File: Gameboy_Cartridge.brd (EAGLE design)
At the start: 51 x 48 mm, 4 parts, among them IC1 AT49F040J

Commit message: Files sent to manufacture
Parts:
- added C1: 20nF, resistor:C0805
- R1: value 47000 -> 47K
- moved R1 45.3 mm to (40.0, 41.6), turned to 180 degrees
- moved IC1 5.52 mm to (38.1, 30.3)
- moved U$2 2.20 mm to (18.9, 23.4)
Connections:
- new net 31: IC1.31, R1.1, U$1.31
- net A: now also IC1.1, U$2.14; no longer IC1.2, U$2.16
- net B: now also IC1.30, U$2.15; no longer IC1.3, U$2.17
- net C: now also IC1.2, U$2.16; no longer IC1.31, R1.1, U$1.31, U$2.14
- net D: now also IC1.3, U$2.17; no longer IC1.30, U$2.15
- net GND: now also C1.2; no longer IC1.1
- net VDD: now also C1.1
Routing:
- net 19: track 0.00 -> 84.5 mm, vias 0 -> 3
- net VDD: track 0.00 -> 81.2 mm
- net 21: track 0.00 -> 78.7 mm
- net 14: track 0.00 -> 68.9 mm, vias 0 -> 2
- net 4: track 0.00 -> 66.5 mm, vias 0 -> 3
- net 30: track 0.00 -> 61.7 mm, vias 0 -> 2
- net GND: track 0.00 -> 59.0 mm, vias 0 -> 4
- net 8: track 0.00 -> 58.2 mm
- net 20: track 0.00 -> 49.4 mm, vias 0 -> 2
- net 26: track 0.00 -> 44.0 mm
- net 18: track 0.00 -> 43.1 mm, vias 0 -> 2
- net 31: track 0.00 -> 42.7 mm
- net 25: track 0.00 -> 42.3 mm
- net E: track 0.00 -> 40.6 mm, vias 0 -> 2
- net 24: track 0.00 -> 40.3 mm
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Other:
- board size 51 x 48 mm -> 49.3 x 48 mm
- board text added: "47417"
- board text added: "Cartridge"
- board text added: "Gameboy"
- board text added: "Homebrew"
- board text added: "goo.gl/Hq5Kc"

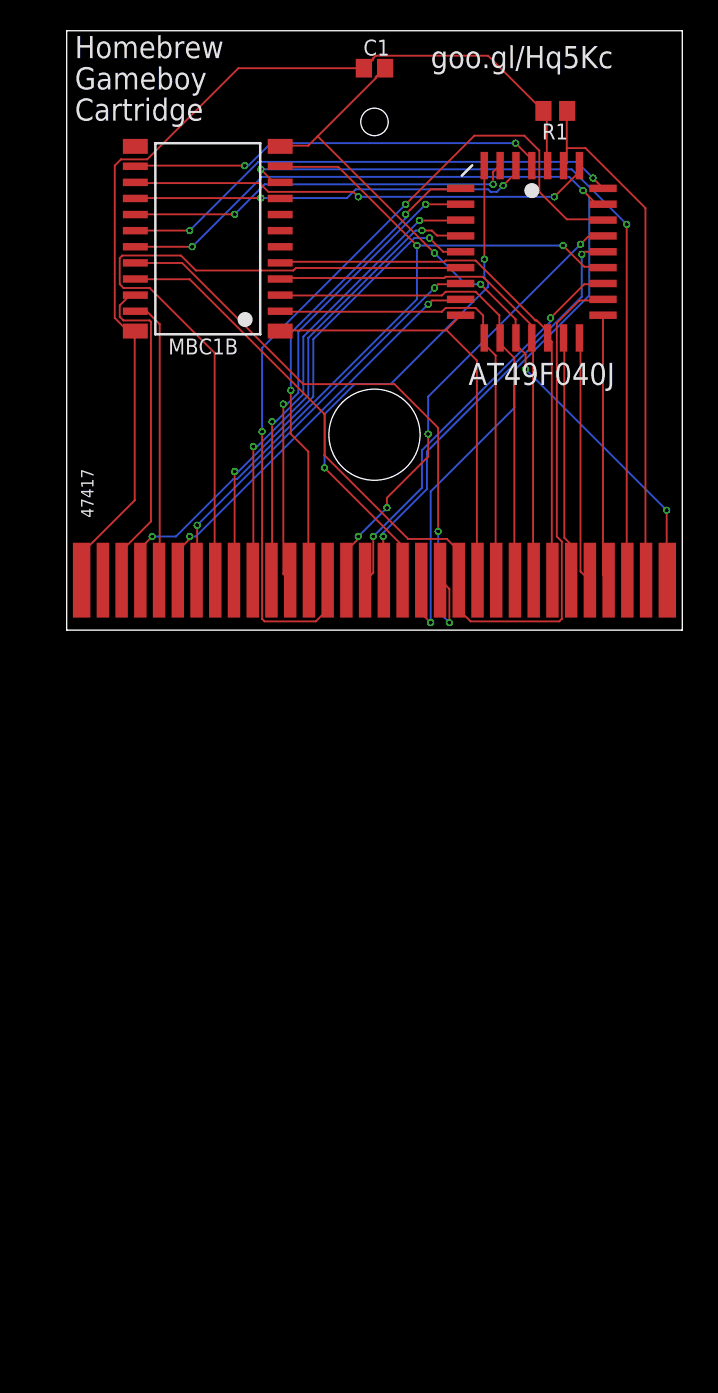
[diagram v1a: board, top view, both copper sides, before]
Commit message: add solder jumpers where traces should be shorted for ROM only operation
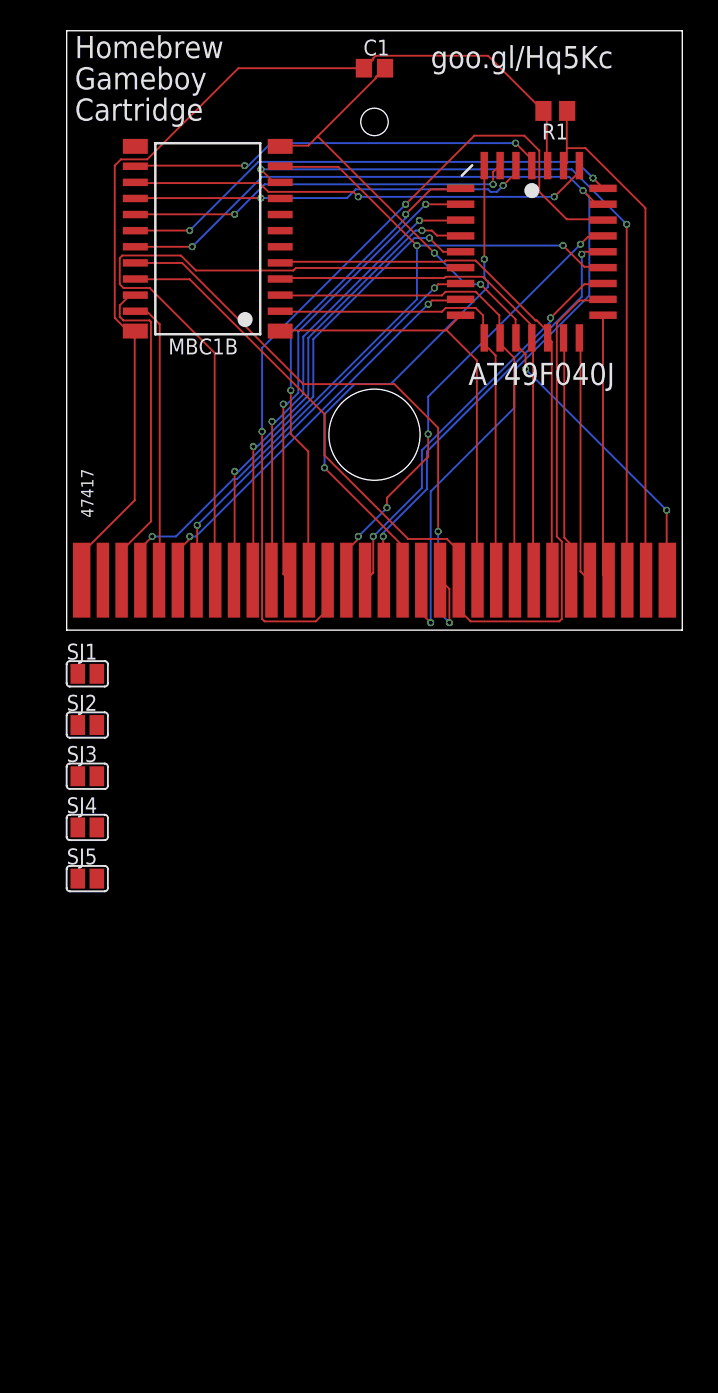
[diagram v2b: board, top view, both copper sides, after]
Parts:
- added SJ1, SJ2, SJ3, SJ4, SJ5: (no value), jumper:SJ
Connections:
- net A: now also SJ1.1
- net B: now also SJ2.1, SJ3.1, SJ4.1
- net GND: now also SJ1.2, SJ2.2, SJ3.2, SJ4.2
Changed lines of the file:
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@@
 <?xml version="1.0" encoding="utf-8"?>
 <!DOCTYPE eagle SYSTEM "eagle.dtd">
-<eagle version="6.1">
+<eagle version="9.3.2">
 <drawing>
 <settings>
 <setting alwaysvectorfont="no"/>
+<setting keepoldvectorfont="yes"/>
 <setting verticaltext="up"/>
 </settings>
@@
 </class>
 </classes>
-<designrules>
+<designrules name="default">
 <description language="de">&lt;b&gt;EAGLE Design Rules&lt;/b&gt;
 &lt;p&gt;
@@
 <param name="dpMaxLengthDifference" value="10mm"/>
 <param name="dpGapFactor" value="2.5"/>
-<param name="checkGrid" value="0"/>
 <param name="checkAngle" value="0"/>
 <param name="checkFont" value="1"/>
 <param name="checkRestrict" value="0"/>
+<param name="checkStop" value="0"/>
+<param name="checkValues" value="0"/>
+<param name="checkNames" value="1"/>
+<param name="checkWireStubs" value="1"/>
+<param name="checkPolygonWidth" value="0"/>
 <param name="useDiameter" value="13"/>
 <param name="maxErrors" value="50"/>
@@
 <pass name="Default">
 <param name="RoutingGrid" value="0.1mm"/>
+<param name="AutoGrid" value="1"/>
+<param name="Efforts" value="0"/>
+<param name="TopRouterVariant" value="1"/>
 <param name="tpViaShape" value="round"/>
 <param name="PrefDir.1" value="*"/>
@@
 </autorouter>
 <elements>
-<element name="U$2" library="gameboy" package="MBC1B" value="MBC1B" x="18.95" y="23.35" rot="R180"/>
-<element name="U$1" library="gameboy" package="CONNECTOR" value="CONNECTOR" x="1.35" y="7"/>
-<element name="R1" library="resistor" package="M0805" value="47K" x="39.98" y="41.58" rot="R180"/>
-<element name="IC1" library="gameboy" package="PLCC32R" value="AT49F040J" x="38.1" y="30.3"/>
-<element name="C1" library="resistor" package="C0805" value="20nF" x="25.5" y="45"/>
+<element name="U$2" library="gameboy" package="MBC1B" value="MBC1B" x="18.95" y="23.35" smashed="yes" rot="R180">
+<attribute name="VALUE" x="14.579996875" y="23.35" size="1.27" layer="21" rot="R180"/>
+</element>
+<element name="U$1" library="gameboy" package="CONNECTOR" value="CONNECTOR" x="1.35" y="7" smashed="yes"/>
+<element name="R1" library="resistor" package="M0805" value="47K" x="39.98" y="41.58" smashed="yes" rot="R180">
+<attribute name="NAME" x="40.996" y="40.564" size="1.27" layer="25" rot="R180"/>
+<attribute name="VALUE" x="40.996" y="43.866" size="1.27" layer="27" rot="R180"/>
+</element>
+<element name="IC1" library="gameboy" package="PLCC32R" value="AT49F040J" x="38.1" y="30.3" smashed="yes">
+<attribute name="VALUE" x="33.02" y="19.632" size="1.778" layer="21"/>
+</element>
+<element name="C1" library="resistor" package="C0805" value="20nF" x="25.5" y="45" smashed="yes">
+<attribute name="NAME" x="24.611" y="46.016" size="1.27" layer="25"/>
+<attribute name="VALUE" x="24.611" y="42.714" size="1.27" layer="27"/>
+</element>
+<element name="SJ1" library="jumper" library_urn="urn:adsk.eagle:library:252" package="SJ" package3d_urn="urn:adsk.eagle:package:15471/1" value="" x="2.5" y="-3.5" smashed="yes">
+<attribute name="NAME" x="0.849" y="-2.357" size="1.27" layer="25" ratio="10"/>
+<attribute name="VALUE" x="2.9001" y="-3.5" size="0.02" layer="27"/>
+</element>
+<element name="SJ2" library="jumper" library_urn="urn:adsk.eagle:library:252" package="SJ" package3d_urn="urn:adsk.eagle:package:15471/1" value="" x="2.5" y="-7.6" smashed="yes">
+<attribute name="NAME" x="0.849" y="-6.457" size="1.27" layer="25" ratio="10"/>
+<attribute name="VALUE" x="2.9001" y="-7.6" size="0.02" layer="27"/>
+</element>
+<element name="SJ3" library="jumper" library_urn="urn:adsk.eagle:library:252" package="SJ" package3d_urn="urn:adsk.eagle:package:15471/1" value="" x="2.5" y="-11.7" smashed="yes">
+<attribute name="NAME" x="0.849" y="-10.557" size="1.27" layer="25" ratio="10"/>
+<attribute name="VALUE" x="2.9001" y="-11.7" size="0.02" layer="27"/>
+</element>
+<element name="SJ4" library="jumper" library_urn="urn:adsk.eagle:library:252" package="SJ" package3d_urn="urn:adsk.eagle:package:15471/1" value="" x="2.5" y="-15.8" smashed="yes">
+<attribute name="NAME" x="0.849" y="-14.657" size="1.27" layer="25" ratio="10"/>
+<attribute name="VALUE" x="2.9001" y="-15.8" size="0.02" layer="27"/>
+</element>
+<element name="SJ5" library="jumper" library_urn="urn:adsk.eagle:library:252" package="SJ" package3d_urn="urn:adsk.eagle:package:15471/1" value="" x="2.5" y="-19.9" smashed="yes">
+<attribute name="NAME" x="0.849" y="-18.757" size="1.27" layer="25" ratio="10"/>
+<attribute name="VALUE" x="2.9001" y="-19.9" size="0.02" layer="27"/>
+</element>
 </elements>
 <signals>
@@
 <via x="48.9" y="9.6" extent="1-16" drill="0.3048"/>
 <via x="37.6" y="20.9" extent="1-16" drill="0.3048"/>
+<contactref element="SJ1" pad="2"/>
+<contactref element="SJ3" pad="2"/>
+<contactref element="SJ4" pad="2"/>
+<contactref element="SJ2" pad="2"/>
+<wire x1="3.262" y1="-3.5" x2="37.6" y2="20.9" width="0" layer="19" extent="1-1"/>
+<wire x1="3.262" y1="-7.6" x2="3.262" y2="-3.5" width="0" layer="19" extent="1-1"/>
+<wire x1="3.262" y1="-11.7" x2="3.262" y2="-7.6" width="0" layer="19" extent="1-1"/>
+<wire x1="3.262" y1="-15.8" x2="3.262" y2="-11.7" width="0" layer="19" extent="1-1"/>
 </signal>
 <signal name="VDD">
@@
 <via x="24.2" y="34.7" extent="1-16" drill="0.3048"/>
 <via x="39.9" y="34.7" extent="1-16" drill="0.3048"/>
+<contactref element="SJ2" pad="1"/>
+<contactref element="SJ3" pad="1"/>
+<contactref element="SJ4" pad="1"/>
+<wire x1="1.738" y1="-7.6" x2="6.4" y2="35.8" width="0" layer="19" extent="1-1"/>
+<wire x1="1.738" y1="-11.7" x2="1.738" y2="-7.6" width="0" layer="19" extent="1-1"/>
+<wire x1="1.738" y1="-15.8" x2="1.738" y2="-11.7" width="0" layer="19" extent="1-1"/>
 </signal>
 <signal name="A">
@@
 <via x="15.1" y="37.2" extent="1-16" drill="0.3048"/>
 <via x="36.8" y="39" extent="1-16" drill="0.3048"/>
+<contactref element="SJ1" pad="1"/>
+<wire x1="1.738" y1="-3.5" x2="6.35" y2="37.15" width="0" layer="19" extent="1-1"/>
 </signal>
 </signals>
+<mfgpreviewcolors>
+<mfgpreviewcolor name="soldermaskcolor" color="0xC8008000"/>
+<mfgpreviewcolor name="silkscreencolor" color="0xFFFEFEFE"/>
+<mfgpreviewcolor name="backgroundcolor" color="0xFF282828"/>
+<mfgpreviewcolor name="coppercolor" color="0xFFFFBF00"/>
+<mfgpreviewcolor name="substratecolor" color="0xFF786E46"/>
+</mfgpreviewcolors>
 </board>
 </drawing>
+<compatibility>
+<note version="8.2" severity="warning">
+Since Version 8.2, EAGLE supports online libraries. The ids
+of those online libraries will not be understood (or retained)
+with this version.
+</note>
+<note version="8.3" severity="warning">
+Since Version 8.3, EAGLE supports URNs for individual library
+assets (packages, symbols, and devices). The URNs of those assets
+will not be understood (or retained) with this version.
+</note>
+<note version="8.3" severity="warning">
+Since Version 8.3, EAGLE supports the association of 3D packages
+with devices in libraries, schematics, and board files. Those 3D
+packages will not be understood (or retained) with this version.
+</note>
+</compatibility>
 </eagle>

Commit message: replace the solder jumper with my new part
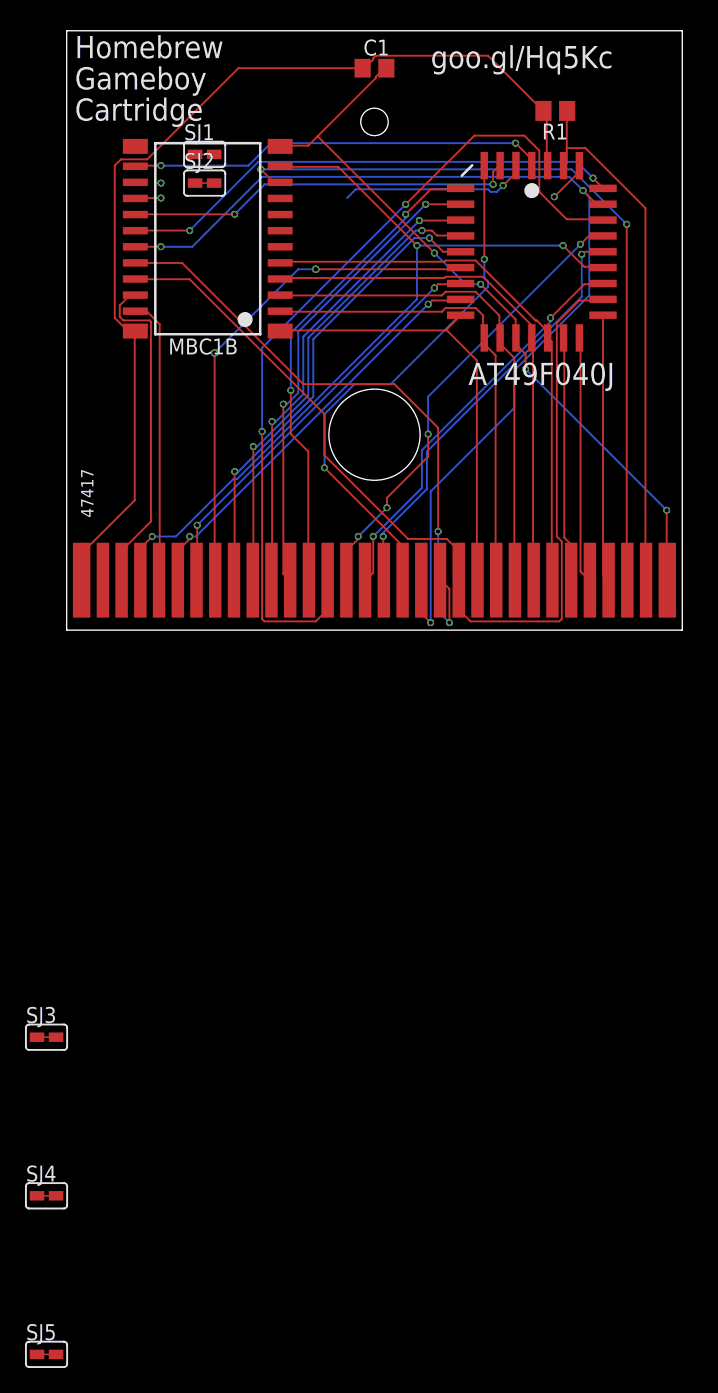
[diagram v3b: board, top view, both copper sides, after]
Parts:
- SJ1, SJ2, SJ3, SJ4, SJ5: value (none) -> SOLDER-JUMPER; device jumper:SJ -> gameboy:SJ
- moved SJ2 44.4 mm to (11.9, 35.8)
- moved SJ1 42.6 mm to (11.9, 38.1)
- moved SJ5 38.2 mm to (-0.76, -58.0)
- moved SJ4 29.7 mm to (-0.76, -45.3)
- moved SJ3 21.2 mm to (-0.76, -32.6)
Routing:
- net B: track 37.4 -> 3.42 mm
- net 8: track 58.2 -> 40.8 mm, vias 0 -> 2
- net C: track 32.1 -> 17.2 mm

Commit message: Fix the connections on the solder jumper
No ERC errors
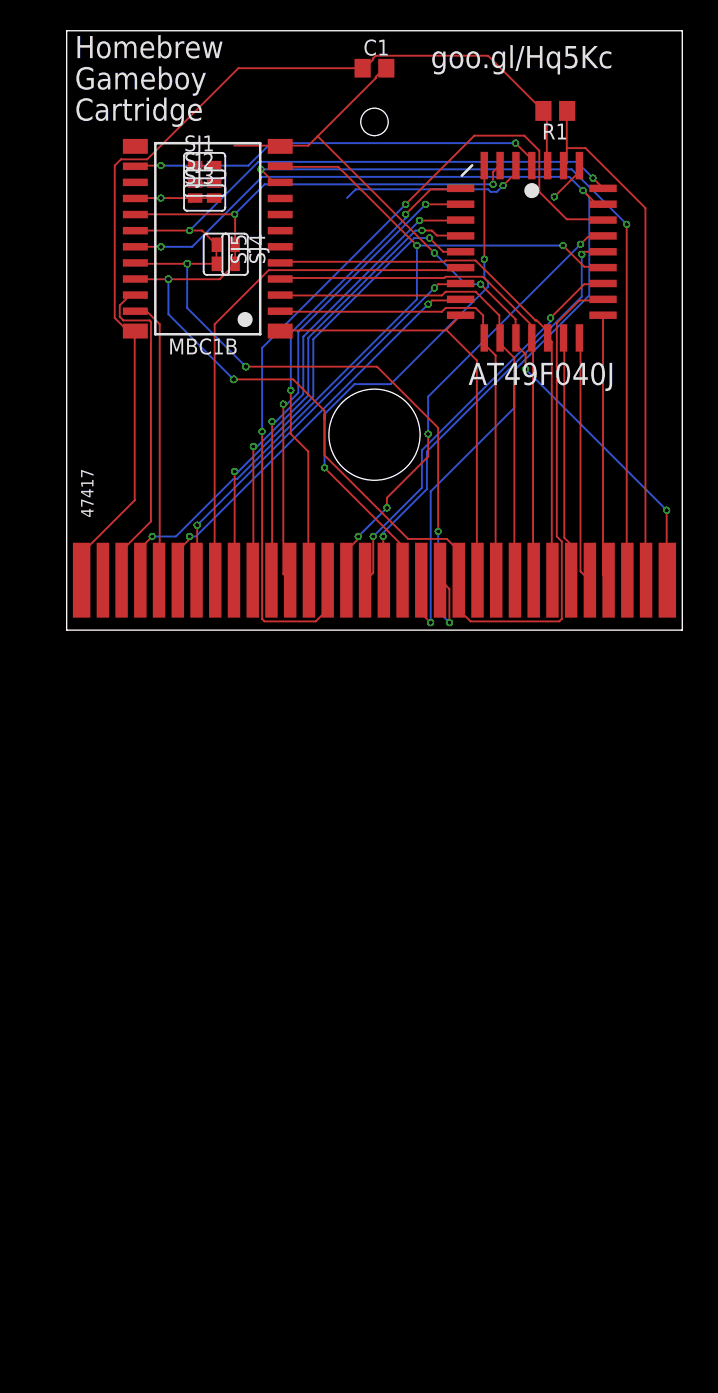
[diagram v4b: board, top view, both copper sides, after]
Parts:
- moved SJ5 89.1 mm to (12.8, 30.1), turned to 270 degrees
- moved SJ4 76.9 mm to (14.3, 30.1), turned to 270 degrees
- moved SJ3 68.4 mm to (11.9, 34.6)
- moved SJ1 0.90 mm to (11.9, 37.2)
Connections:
- net 20: now also SJ5.2
- net 21: now also SJ4.2
- net B: no longer SJ3.1, SJ4.1
- net C: now also SJ3.1
- net D: now also SJ4.1
- net E: now also SJ5.1
- net GND: no longer SJ4.2
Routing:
- net 21: track 78.7 -> 86.8 mm, vias 0 -> 2
- net 20: track 49.4 -> 53.9 mm, vias 2 -> 4
- net GND: track 59.1 -> 62.8 mm
- net C: track 17.2 -> 19.9 mm
- net E: track 40.6 -> 43.2 mm
- net D: track 31.4 -> 33.9 mm
- net 8: track 40.8 -> 42.4 mm, vias 2 -> 0
- net B: vias 2 -> 1

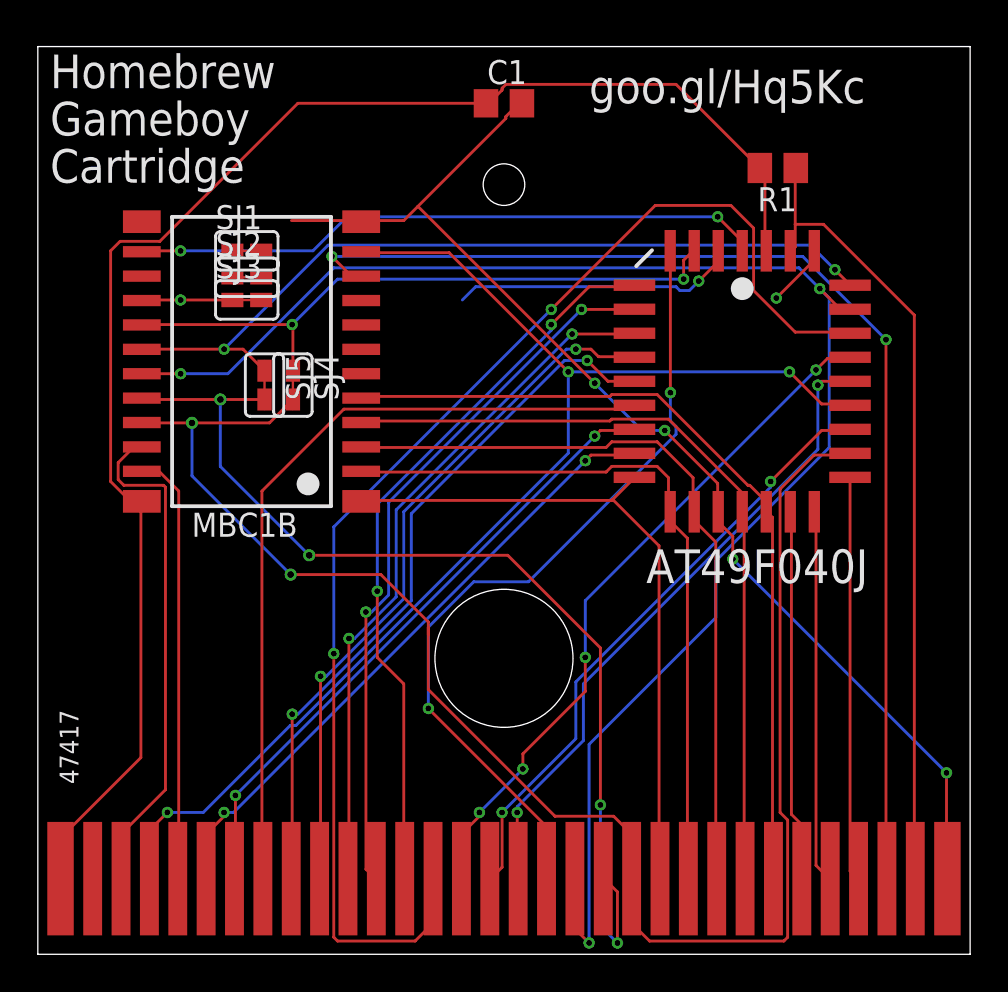
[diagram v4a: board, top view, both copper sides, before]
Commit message: Ripup all traces. Route most of it
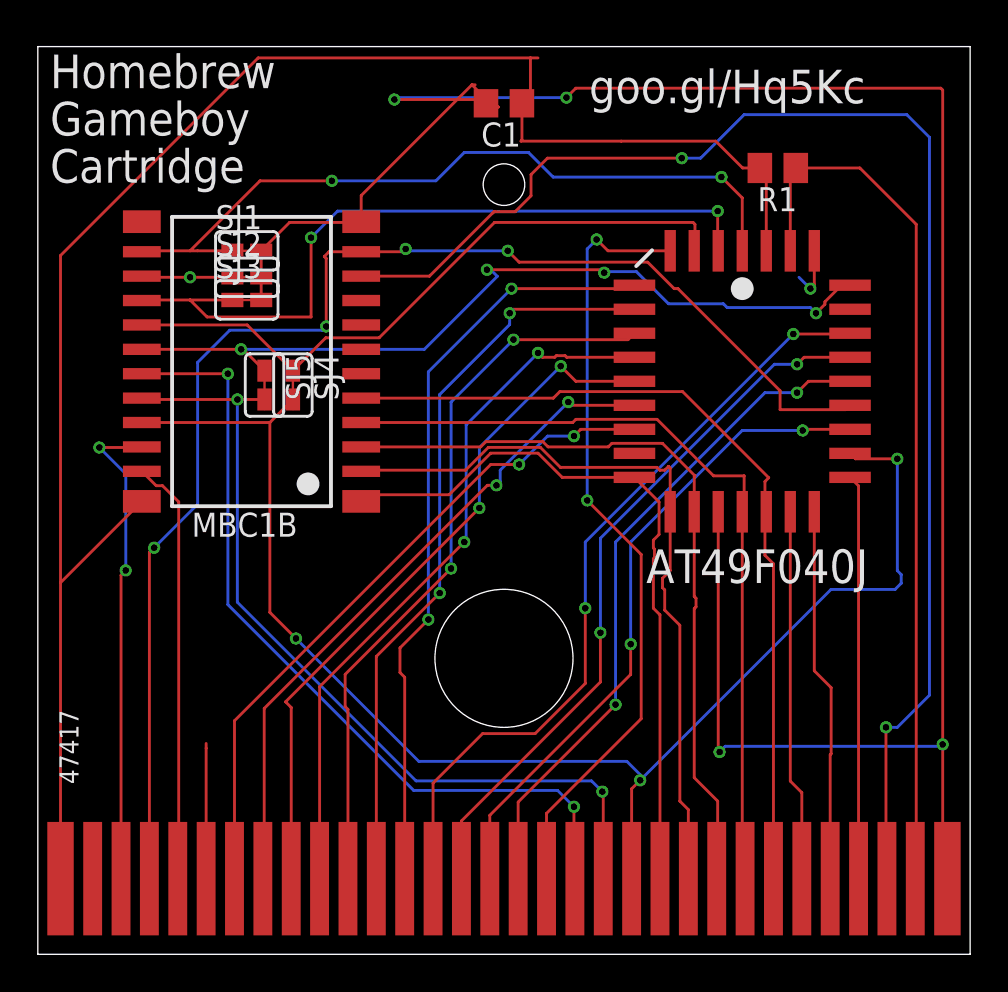
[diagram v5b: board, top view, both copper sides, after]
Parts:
- turned C1 to 180 degrees
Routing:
- net GND: track 62.8 -> 121.9 mm
- net 19: track 84.5 -> 43.3 mm, vias 3 -> 2
- net 14: track 68.9 -> 41.3 mm
- net 6: track 33.5 -> 7.15 mm, vias 2 -> 0
- net C: track 19.9 -> 40.0 mm
- net 30: track 61.7 -> 76.5 mm
- net 21: track 86.8 -> 74.8 mm, vias 2 -> 3
- net VDD: track 81.2 -> 91.0 mm
- net 20: track 53.9 -> 45.3 mm, vias 4 -> 2
- net 8: track 42.4 -> 35.7 mm, vias 0 -> 2
- net A: track 33.6 -> 40.0 mm
- net 4: track 66.5 -> 72.2 mm, vias 3 -> 4
- net B: track 3.42 -> 7.75 mm, vias 1 -> 2
- net 31: track 42.6 -> 46.8 mm
- net 16: track 32.6 -> 35.0 mm
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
